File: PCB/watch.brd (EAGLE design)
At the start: 81.1 x 53.1 mm, 58 parts, among them IC1 ISL1209, J2 USB-MICROB, Q1 32.768 KHz, T1 BC850, U2 MKL27Z256VLH4

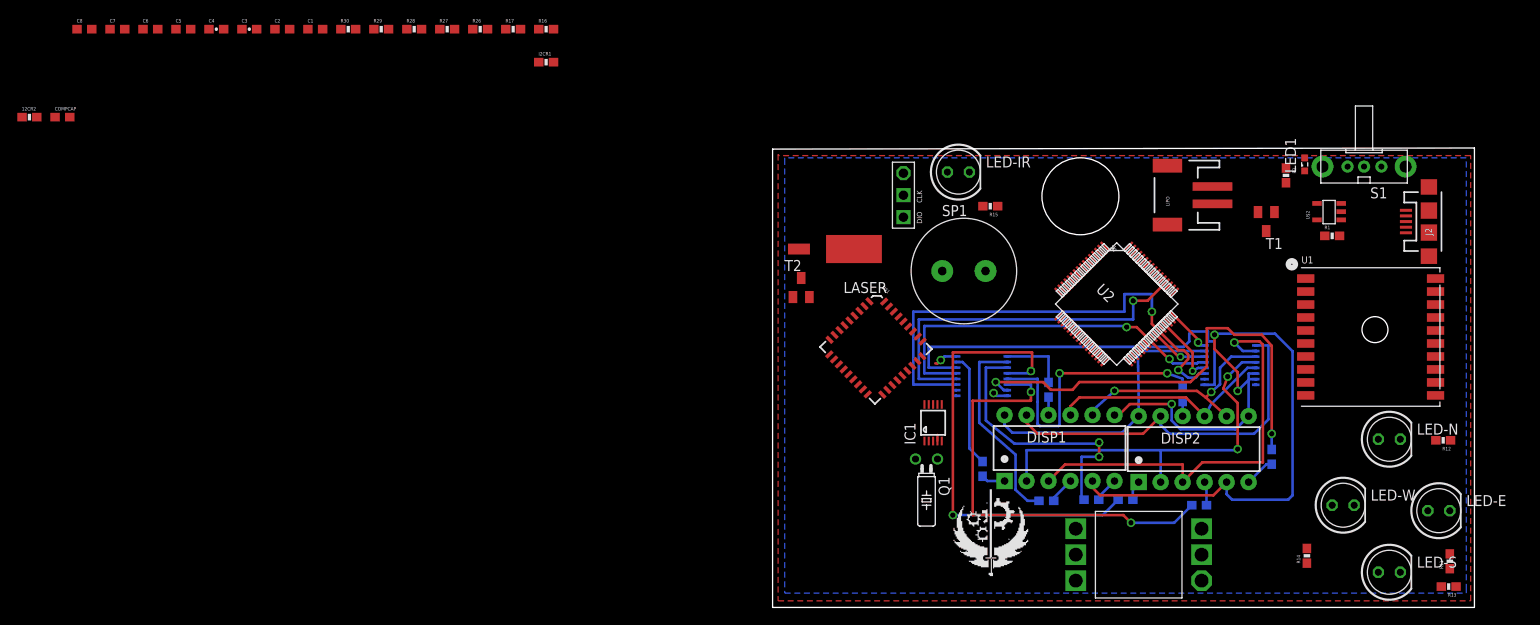
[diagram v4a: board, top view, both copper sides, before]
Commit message: wired more resistors and traces
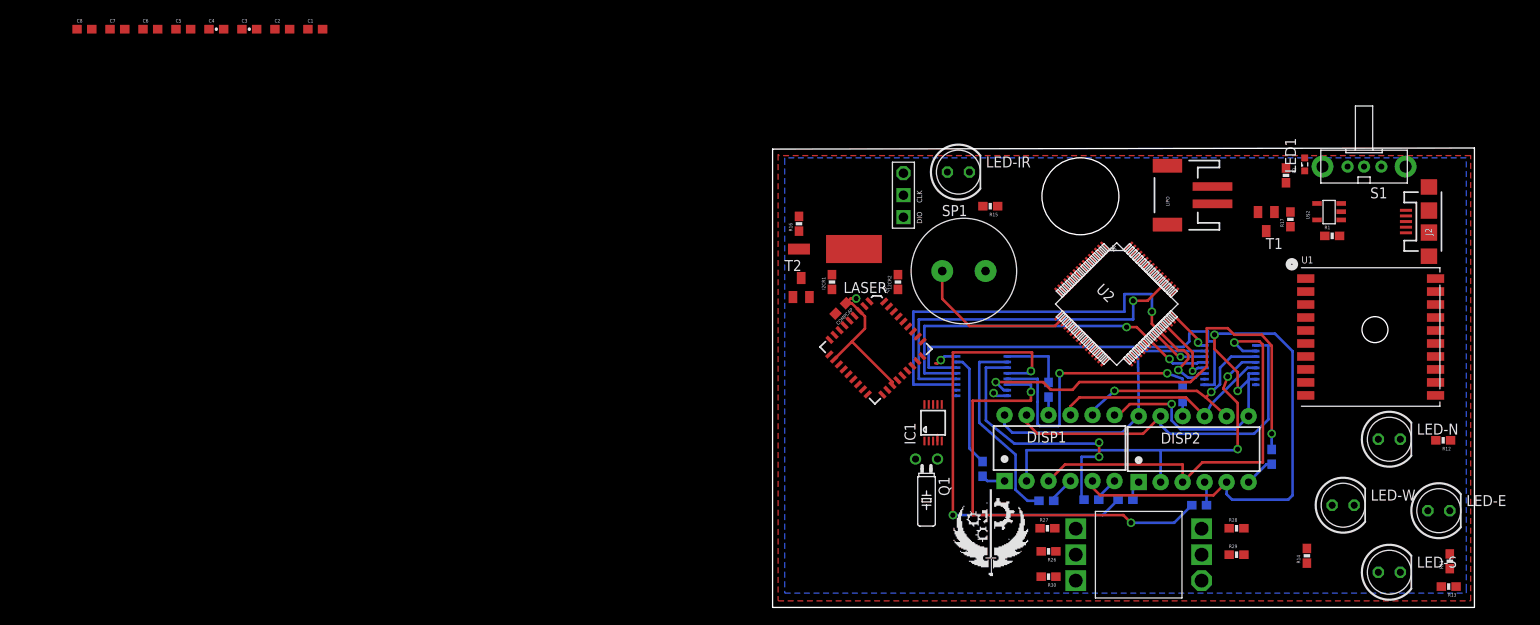
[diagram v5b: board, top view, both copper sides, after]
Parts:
- moved R29 116.0 mm to (64.5, 13.0)
- moved R28 111.1 mm to (64.5, 16.0)
- moved R30 102.7 mm to (42.8, 10.4), turned to 180 degrees
- moved 12CR2 102.1 mm to (25.4, 44.5), turned to 90 degrees
- moved COMPCAP 92.6 mm to (18.8, 41.4), turned to 225 degrees
- moved R17 92.4 mm to (70.7, 51.7), turned to 90 degrees
- moved R27 90.2 mm to (42.7, 16.0)
- moved R26 89.2 mm to (42.8, 13.3), turned to 180 degrees
- moved I2CR1 41.7 mm to (17.8, 44.5), turned to 90 degrees
- moved R16 36.9 mm to (14.0, 51.2), turned to 90 degrees
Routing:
- net PTE30: track 0.00 -> 18.7 mm
- net V+: track 7.66 -> 25.3 mm, vias 2 -> 3

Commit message: wired charging circuit
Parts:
- moved Q1 44.4 mm to (67.7, 45.3), turned to 270 degrees
- moved IC1 38.9 mm to (64.0, 46.0), turned to 90 degrees
- moved LED1 1.17 mm to (72.1, 56.9), turned to 270 degrees
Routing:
- net N$4: track 0.00 -> 25.8 mm
- net PTE0: track 0.00 -> 23.7 mm
- net PTE20: track 0.00 -> 17.6 mm
- net N$7: track 0.00 -> 8.54 mm
- net N$39: track 0.00 -> 5.73 mm
- net N$3: track 0.00 -> 5.35 mm
- net N$8: track 0.00 -> 2.22 mm
- net N$44: track 0.00 -> 2.04 mm
- net N$43: track 0.00 -> 1.94 mm
- net N$5: track 0.00 -> 1.93 mm
- net GND: track 2.75 -> 4.61 mm, vias 1 -> 2
- net N$42: track 0.00 -> 1.85 mm

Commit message: moved clock, rewired gps
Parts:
- moved R17 58.3 mm to (13.3, 41.3)
- moved T1 54.1 mm to (14.2, 45.3), turned to 0 degrees
- moved T2 52.4 mm to (66.5, 41.8), turned to 270 degrees
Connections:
- net PTB3: no longer U1.P$5
- net PTD3: now also U1.P$5
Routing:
- net PTE0: track 23.7 -> 0.00 mm
- net N$41: track 0.00 -> 9.08 mm
- net PTC9: track 0.00 -> 6.97 mm
- net PTC8: track 0.00 -> 6.56 mm
- net V+: track 25.3 -> 31.5 mm, vias 3 -> 4
- net N$6: track 0.00 -> 6.13 mm
- net N$40: track 0.00 -> 2.07 mm

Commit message: rewired gps
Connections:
- new net PTC10: U1.P$5, U2.55
- new net PTC11: U1.P$9, U2.56
- net PTA19: no longer U1.P$9
- net PTD3: no longer U1.P$5
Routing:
- net PTC11: track 0.00 -> 31.5 mm
- net PTC10: track 0.00 -> 26.6 mm
- net V+: track 31.5 -> 35.2 mm, vias 4 -> 5
- net PTB3: track 0.00 -> 1.65 mm
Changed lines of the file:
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@@
 <wire x1="61.8949" y1="44.974" x2="62.611" y2="44.2579" width="0.254" layer="1"/>
 <wire x1="62.611" y1="44.2579" x2="62.611" y2="42.799" width="0.254" layer="1"/>
+<wire x1="72.51" y1="40.35" x2="71.156" y2="40.35" width="0.254" layer="1"/>
+<wire x1="71.156" y1="40.35" x2="70.231" y2="41.275" width="0.254" layer="1"/>
+<via x="70.231" y="41.275" extent="1-16" drill="0.6" shape="square"/>
+<wire x1="70.231" y1="41.275" x2="70.231" y2="41.783" width="0.254" layer="16"/>
+<wire x1="70.231" y1="41.783" x2="69.85" y2="42.164" width="0.254" layer="16"/>
 <wire x1="65.382" y1="42.799" x2="66.1211" y2="45.974" width="0" layer="19" extent="1-1"/>
 <wire x1="17.78" y1="45.3" x2="19.939" y2="42.545" width="0" layer="19" extent="1-1"/>
@@
 <wire x1="57.302134375" y1="40.584171875" x2="61.976" y2="43.307" width="0" layer="19" extent="1-16"/>
 <wire x1="25.4" y1="45.3" x2="20.574" y2="42.545" width="0" layer="19" extent="1-1"/>
-<wire x1="72.51" y1="40.35" x2="65.448" y2="42.733" width="0" layer="19" extent="1-1"/>
 <wire x1="48.640065625" y1="35.98796875" x2="57.302134375" y2="40.584171875" width="0" layer="19" extent="1-1"/>
 <wire x1="45.104521875" y1="44.29648125" x2="48.640065625" y2="35.98796875" width="0" layer="19" extent="1-1"/>
@@
 <signal name="PTA19">
 <contactref element="U2" pad="33"/>
-<contactref element="U1" pad="P$9"/>
-<wire x1="51.998825" y1="35.2808625" x2="72.51" y2="32.85" width="0" layer="19" extent="1-1"/>
 </signal>
 <signal name="N$6">
@@
 <signal name="PTB3">
 <contactref element="U2" pad="38"/>
+<wire x1="53.7665875" y1="37.048628125" x2="54.991" y2="35.941" width="0.254" layer="1"/>
 </signal>
 <signal name="PTE30">
@@
 <contactref element="U$1" pad="32"/>
 <contactref element="IC1" pad="8"/>
+<wire x1="61.8949" y1="45.974" x2="57.2118875" y2="45.974" width="0.254" layer="1"/>
+<wire x1="57.2118875" y1="45.974" x2="55.887921875" y2="44.650034375" width="0.254" layer="1"/>
 <wire x1="26.030421875" y1="39.880965625" x2="55.887921875" y2="44.650034375" width="0" layer="19" extent="1-1"/>
 <wire x1="25.4" y1="43.6" x2="26.030421875" y2="39.880965625" width="0" layer="19" extent="1-1"/>
-<wire x1="61.8949" y1="45.974" x2="57.2118875" y2="45.974" width="0.254" layer="1"/>
-<wire x1="57.2118875" y1="45.974" x2="55.887921875" y2="44.650034375" width="0.254" layer="1"/>
 </signal>
 <signal name="PTC9">
@@
 <contactref element="U$1" pad="36"/>
 <contactref element="IC1" pad="7"/>
+<wire x1="61.8949" y1="46.474" x2="57.00478125" y2="46.474" width="0.254" layer="1"/>
+<wire x1="57.00478125" y1="46.474" x2="55.53436875" y2="45.0035875" width="0.254" layer="1"/>
 <wire x1="23.8115375" y1="42.18673125" x2="55.53436875" y2="45.0035875" width="0" layer="19" extent="1-1"/>
 <wire x1="17.78" y1="43.6" x2="23.8115375" y2="42.18673125" width="0" layer="19" extent="1-1"/>
-<wire x1="61.8949" y1="46.474" x2="57.00478125" y2="46.474" width="0.254" layer="1"/>
-<wire x1="57.00478125" y1="46.474" x2="55.53436875" y2="45.0035875" width="0.254" layer="1"/>
 </signal>
 <signal name="PTE20">
@@
 <contactref element="U2" pad="60"/>
 <contactref element="LED-E" pad="A"/>
-<contactref element="U1" pad="P$5"/>
-<wire x1="86.614" y1="18.034" x2="72.51" y2="38.85" width="0" layer="19" extent="1-1"/>
-<wire x1="53.413034375" y1="47.124921875" x2="72.51" y2="38.85" width="0" layer="19" extent="1-1"/>
+<wire x1="53.413034375" y1="47.124921875" x2="86.614" y2="18.034" width="0" layer="19" extent="1-1"/>
 </signal>
 <signal name="PTD2">
@@
 <wire x1="67.984" y1="23.407" x2="65.913" y2="21.336" width="0.3048" layer="16"/>
 </signal>
+<signal name="PTC10">
+<contactref element="U1" pad="P$5"/>
+<contactref element="U2" pad="55"/>
+<wire x1="55.18081875" y1="45.357140625" x2="57.575678125" y2="47.752" width="0.254" layer="1"/>
+<wire x1="57.575678125" y1="47.752" x2="63.754" y2="47.752" width="0.254" layer="1"/>
+<wire x1="63.754" y1="47.752" x2="63.754" y2="43.815" width="0.254" layer="1"/>
+<wire x1="63.754" y1="43.815" x2="63.881" y2="43.688" width="0.254" layer="1"/>
+<wire x1="63.881" y1="43.688" x2="66.675" y2="43.688" width="0.254" layer="1"/>
+<wire x1="66.675" y1="43.688" x2="66.675" y2="40.132" width="0.254" layer="1"/>
+<wire x1="72.009" y1="38.608" x2="72.251" y2="38.85" width="0.254" layer="1"/>
+<wire x1="72.251" y1="38.85" x2="72.51" y2="38.85" width="0.254" layer="1"/>
+<wire x1="72.009" y1="38.608" x2="70.485" y2="40.132" width="0.254" layer="1"/>
+<wire x1="70.485" y1="40.132" x2="66.675" y2="40.132" width="0.254" layer="1"/>
+</signal>
+<signal name="PTC11">
+<contactref element="U1" pad="P$9"/>
+<contactref element="U2" pad="56"/>
+<wire x1="72.51" y1="32.85" x2="69.215" y2="36.145" width="0.254" layer="1"/>
+<wire x1="69.215" y1="36.145" x2="69.215" y2="37.338" width="0.254" layer="1"/>
+<wire x1="69.215" y1="37.338" x2="66.675" y2="39.878" width="0.254" layer="1"/>
+<wire x1="66.675" y1="39.878" x2="59.436" y2="39.878" width="0.254" layer="1"/>
+<wire x1="59.436" y1="39.878" x2="57.531" y2="41.783" width="0.254" layer="1"/>
+<wire x1="57.531" y1="41.783" x2="53.467" y2="41.783" width="0.254" layer="1"/>
+<wire x1="53.467" y1="41.783" x2="53.086" y2="41.402" width="0.254" layer="1"/>
+<wire x1="53.086" y1="41.402" x2="51.308" y2="41.402" width="0.254" layer="1"/>
+<wire x1="51.308" y1="41.402" x2="51.308" y2="42.1914625" width="0.254" layer="1"/>
+<wire x1="51.308" y1="42.1914625" x2="54.827246875" y2="45.710709375" width="0.254" layer="1"/>
+</signal>
 </signals>
